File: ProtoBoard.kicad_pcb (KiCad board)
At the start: 4 copper layers, 56 x 48 mm, 96 parts, among them J1 Conn_01x03_Female, J10 Conn_01x08_Female, J12 Conn_01x08_Female, J2 TYPE-C-31-M-12, J3 Conn_01x04_Female, J4 Conn_01x10_Female, J5 Conn_01x05_Female, J6 Conn_01x05_Female, J7 Conn_01x10_Female, J8 Conn_01x05_Female, J9 Conn_01x10_Female, Q1 HX2300A, Q2 HX2300A, SW1 SW_Push, SW2 SW_Push, U1 ESP32-S3-MINI-1, U10 DRV2605LDGS, U11 DRV2605LDGS, U12 DRV2605LDGS, U13 DRV2605LDGS, U14 DRV2605LDGS, U2 CD74HC4067SM, U3 LM1084-5.0, U4 HY2120, U5 WS2812-2020, U6 LM1084-3.3, U7 TCA9548ARGER, U8 DRV2605LDGS, U9 DRV2605LDGS

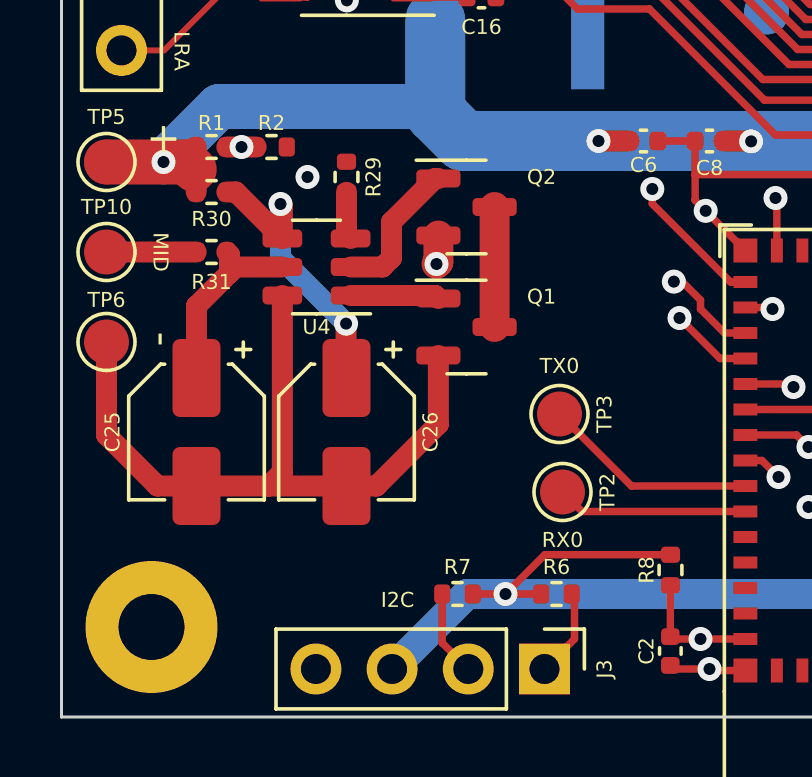
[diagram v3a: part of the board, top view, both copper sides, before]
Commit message: Fix bms + a bit clearer schematic
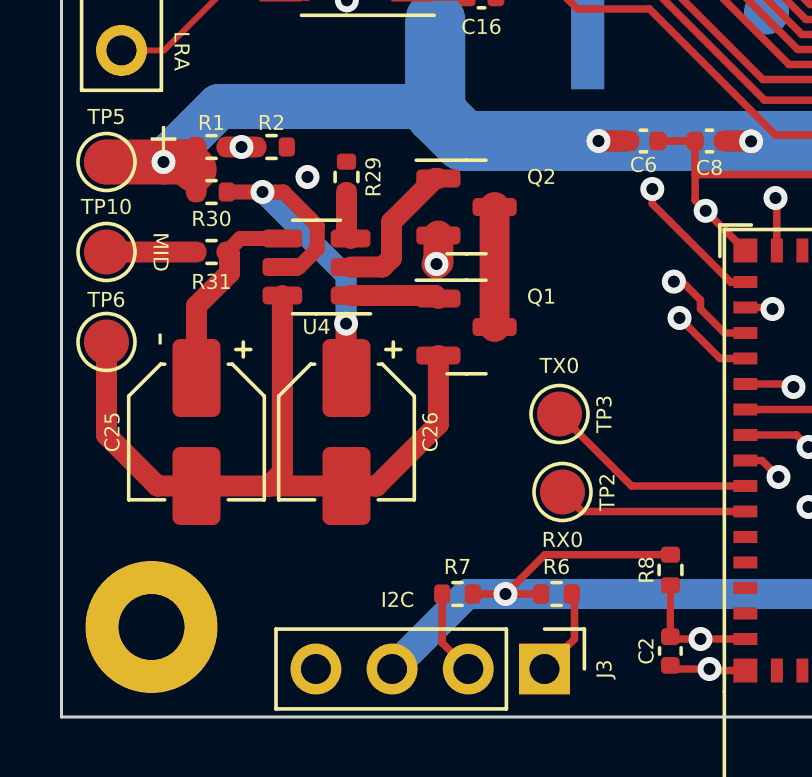
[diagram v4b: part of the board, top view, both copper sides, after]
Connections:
- U4 pad 4: Net-(C26-Pad1) -> /HY_VDD
- U4 pad 5: /HY_VDD -> Net-(C26-Pad1)
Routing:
- net Net-(C26-Pad1): track 10.4 -> 13.0 mm
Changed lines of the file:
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@@
   (net 109 "Net-(Q1-Pad3)")
   (net 110 "/OC")
-  (net 111 "Net-(R29-Pad2)")
+  (net 111 "Net-(U4-Pad3)")
   (net 112 "/MID_BAT")
   (net 113 "unconnected-(U1-Pad41)")
@@
       (net 1 "GND") (pintype "passive"))
     (pad "2" smd roundrect locked (at 0.51 0 270) (size 0.54 0.64) (layers "F.Cu" "F.Paste" "F.Mask") (roundrect_rratio 0.25)
-      (net 111 "Net-(R29-Pad2)") (pintype "passive"))
+      (net 111 "Net-(U4-Pad3)") (pintype "passive"))
     (model "${KICAD6_3DMODEL_DIR}/Resistor_SMD.3dshapes/R_0402_1005Metric.wrl"
       (offset (xyz 0 0 0))
@@
       (net 110 "/OC") (pinfunction "OC") (pintype "output"))
     (pad "3" smd roundrect locked (at -1.1375 0.95 180) (size 1.325 0.6) (layers "F.Cu" "F.Paste" "F.Mask") (roundrect_rratio 0.25)
-      (net 111 "Net-(R29-Pad2)") (pinfunction "CS") (pintype "input"))
+      (net 111 "Net-(U4-Pad3)") (pinfunction "CS") (pintype "input"))
     (pad "4" smd roundrect locked (at 1.1375 0.95 180) (size 1.325 0.6) (layers "F.Cu" "F.Paste" "F.Mask") (roundrect_rratio 0.25)
-      (net 107 "Net-(C26-Pad1)") (pinfunction "VC") (pintype "input"))
+      (net 105 "/HY_VDD") (pinfunction "VC") (pintype "input"))
     (pad "5" smd roundrect locked (at 1.1375 0 180) (size 1.325 0.6) (layers "F.Cu" "F.Paste" "F.Mask") (roundrect_rratio 0.25)
-      (net 105 "/HY_VDD") (pinfunction "VDD") (pintype "power_in"))
+      (net 107 "Net-(C26-Pad1)") (pinfunction "VDD") (pintype "power_in"))
     (pad "6" smd roundrect locked (at 1.1375 -0.95 180) (size 1.325 0.6) (layers "F.Cu" "F.Paste" "F.Mask") (roundrect_rratio 0.25)
       (net 106 "-BATT") (pinfunction "VSS") (pintype "power_in"))
@@
     (pts (xy 47.65 59.75) (xy 103.65 59.75))
     (height -9.5)
-    (gr_text "56.0000 mm" (at 75.65 49.1) (layer "Margin")
+    (gr_text "56,0000 mm" (at 75.65 49.1) (layer "Margin")
       (effects (font (size 1 1) (thickness 0.15)))
     )
@@
     (pts (xy 47.65 109.75) (xy 47.65 61.75))
     (height -3.5)
-    (gr_text "48.0000 mm" (at 43 85.75 90) (layer "Margin")
+    (gr_text "48,0000 mm" (at 43 85.75 90) (layer "Margin")
       (effects (font (size 1 1) (thickness 0.15)))
     )
@@
   (segment (start 90.135 97.1) (end 90.135 97.965) (width 0.25) (layer "F.Cu") (net 2))
   (segment (start 61.36 105.65) (end 62.45 105.65) (width 0.25) (layer "F.Cu") (net 2))
-  (segment (start 62.45 105.45) (end 62.45 105.65) (width 0.2) (layer "F.Cu") (net 2))
   (segment (start 72.64 83.25) (end 73.44 82.45) (width 0.25) (layer "F.Cu") (net 2))
   (segment (start 53.75 82.75) (end 54.75 83.75) (width 0.25) (layer "F.Cu") (net 2))
@@
   (segment (start 92.25188 80.94812) (end 93.547179 80.94812) (width 0.25) (layer "In1.Cu") (net 104))
   (segment (start 85.45 100.35) (end 87.85 97.95) (width 0.25) (layer "In1.Cu") (net 104))
-  (segment (start 55.0125 94.75) (end 53.45 94.75) (width 0.7) (layer "F.Cu") (net 105))
+  (segment (start 53.61 93.8) (end 53.16 94.25) (width 0.5) (layer "F.Cu") (net 105))
+  (segment (start 55.0125 93.8) (end 53.61 93.8) (width 0.5) (layer "F.Cu") (net 105))
   (segment (start 52.15 98.45) (end 52.15 96.05) (width 0.7) (layer "F.Cu") (net 105))
   (segment (start 53.25 94.34) (end 53.16 94.25) (width 0.7) (layer "F.Cu") (net 105))
-  (segment (start 53.45 94.75) (end 53.25 94.95) (width 0.7) (layer "F.Cu") (net 105))
   (segment (start 53.25 94.95) (end 53.25 94.34) (width 0.7) (layer "F.Cu") (net 105))
   (segment (start 52.15 96.05) (end 53.25 94.95) (width 0.7) (layer "F.Cu") (net 105))
@@
   (segment (start 55.0125 101.5875) (end 54.55 102.05) (width 0.7) (layer "F.Cu") (net 106))
   (segment (start 52.15 102.05) (end 54.55 102.05) (width 0.7) (layer "F.Cu") (net 106))
+  (segment (start 55.05 92.25) (end 54.35 92.25) (width 0.5) (layer "F.Cu") (net 107))
   (segment (start 57.135875 96.637316) (end 57.135875 98.435875) (width 0.7) (layer "F.Cu") (net 107))
-  (segment (start 55.0125 93.8) (end 55.0125 92.7125) (width 0.7) (layer "F.Cu") (net 107))
-  (segment (start 53.16 92.25) (end 53.4625 92.25) (width 0.7) (layer "F.Cu") (net 107))
+  (segment (start 55.573528 94.75) (end 56.175 94.148528) (width 0.5) (layer "F.Cu") (net 107))
+  (segment (start 56.175 94.148528) (end 56.175 93.375) (width 0.5) (layer "F.Cu") (net 107))
   (segment (start 57.135875 98.435875) (end 57.15 98.45) (width 0.7) (layer "F.Cu") (net 107))
-  (segment (start 55.0125 92.7125) (end 54.95 92.65) (width 0.7) (layer "F.Cu") (net 107))
-  (segment (start 53.4625 92.25) (end 55.0125 93.8) (width 0.7) (layer "F.Cu") (net 107))
+  (segment (start 55.0125 94.75) (end 55.573528 94.75) (width 0.5) (layer "F.Cu") (net 107))
+  (segment (start 54.35 92.25) (end 53.16 92.25) (width 0.5) (layer "F.Cu") (net 107))
+  (segment (start 56.175 93.375) (end 55.05 92.25) (width 0.5) (layer "F.Cu") (net 107))
+  (via (at 54.35 92.25) (size 0.8) (drill 0.4) (layers "F.Cu" "B.Cu") (net 107))
   (via (at 57.135875 96.637316) (size 0.8) (drill 0.4) (layers "F.Cu" "B.Cu") (net 107))
-  (via (at 54.95 92.65) (size 0.8) (drill 0.4) (layers "F.Cu" "B.Cu") (net 107))
-  (segment (start 54.95 92.65) (end 54.95 94.451441) (width 0.7) (layer "B.Cu") (net 107))
-  (segment (start 54.95 94.451441) (end 57.135875 96.637316) (width 0.7) (layer "B.Cu") (net 107))
+  (segment (start 57.135875 96.637316) (end 57.135875 95.035875) (width 0.7) (layer "B.Cu") (net 107))
+  (segment (start 57.135875 95.035875) (end 54.35 92.25) (width 0.7) (layer "B.Cu") (net 107))
   (segment (start 57.2875 95.7) (end 60.1125 95.7) (width 0.7) (layer "F.Cu") (net 108))
   (segment (start 60.1125 95.7) (end 60.2125 95.8) (width 0.7) (layer "F.Cu") (net 108))
@@
     (connect_pads (clearance 0))
     (min_thickness 0.254)
-    (keepout (tracks not_allowed) (vias not_allowed) (pads not_allowed ) (copperpour not_allowed) (footprints allowed))
+    (keepout (tracks not_allowed) (vias not_allowed) (pads not_allowed) (copperpour not_allowed) (footprints allowed))
     (fill (thermal_gap 0.508) (thermal_bridge_width 0.508))
     (polygon
